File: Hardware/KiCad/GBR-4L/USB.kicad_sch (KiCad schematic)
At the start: 0 parts

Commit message: Add USB hub schematic
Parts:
- added C1: 4.7nF 1kV, Capacitor_SMD:C_1206_3216Metric, symbol Device:C
- added C10, C2, C3, C7, C8, C9: 100nF, Capacitor_SMD:C_0603_1608Metric, symbol Device:C
- added C11: 4.7uF, Capacitor_SMD:C_0805_2012Metric, symbol Device:C
- added C4, C5: 12pF C0G, Capacitor_SMD:C_0603_1608Metric, symbol Device:C
- added C6: 1uF, Capacitor_SMD:C_0603_1608Metric, symbol Device:C
- added J1: USB4105-GF-A, Connector_USB:USB_C_Receptacle_GCT_USB4105-xx-A_16P_TopMnt_Horizontal, symbol Connector:USB_C_Receptacle_USB2.0_16P
- added R1, R2: 5.1k 1%, Resistor_SMD:R_0603_1608Metric, symbol Device:R
- added R3: 1M, Resistor_SMD:R_0603_1608Metric, symbol Device:R
- added R4, R5: 100k 1%, Resistor_SMD:R_0603_1608Metric, symbol Device:R
- added R6: 12.0k 1%, Resistor_SMD:R_0603_1608Metric, symbol Device:R
- added R7: 10k, Resistor_SMD:R_0603_1608Metric, symbol Device:R
- added U1: USBLC6-2SC6, Package_TO_SOT_SMD:SOT-23-6, symbol Power_Protection:USBLC6-2SC6
- added U2: USB2514Bi-I/M2, Package_DFN_QFN:QFN-36-1EP_6x6mm_P0.5mm_EP4.1x4.1mm_ThermalVias, symbol Interface_USB:USB2514B_Bi
- added Y1: 24MHz, symbol Device:Crystal
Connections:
- new net +3V3_SYS: C10.1, C11.1, C7.1, C8.1, C9.1, R7.1, U2.10 (VDDA33), U2.15 (VDD33), U2.23 (VDD33), U2.29 (VDDA33), U2.36 (VDDA33), U2.5 (VDDA33)
- new net GND: C1.2, C10.2, C11.2, C2.2, C3.2, C4.2, C5.2, C6.2, C7.2, C8.2, C9.2, J1.A1 (GND), J1.A12 (GND), J1.B1 (GND), J1.B12 (GND), R1.2, R2.2, R3.2, R5.2, R6.2, U1.2 (GND), U2.37 (VSS)
- new net HUB_CRFILT: C2.1, U2.14 (CRFILT)
- new net HUB_PLLFILT: C3.1, U2.34 (PLLFILT)
- new net HUB_RBIAS: R6.1, U2.35 (RBIAS)
- new net HUB_RESET#: C6.1, R7.2, U2.26 (RESET_N)
- new net HUB_XTALIN: C4.1, U2.33 (XTALIN/CLKIN), Y1.1
- new net HUB_XTALOUT: C5.1, U2.32 (XTALOUT), Y1.2
- new net USB_CC1: J1.A5 (CC1), R1.1
- new net USB_CC2: J1.B5 (CC2), R2.1
- new net USB_M1_D+: U2.2 (USBDP_DN1/PRT_DIS_P1)
- new net USB_M1_D-: U2.1 (USBDM_DN1/PRT_DIS_M1)
- new net USB_M2_D+: U2.4 (USBDP_DN2/PRT_DIS_P2)
- new net USB_M2_D-: U2.3 (USBDM_DN2/PRT_DIS_M2)
- new net USB_M3_D+: U2.7 (USBDP_DN3/PRT_DIS_P3)
- new net USB_M3_D-: U2.6 (USBDM_DN3/PRT_DIS_M3)
- new net USB_M4_D+: U2.9 (USBDP_DN4/PRT_DIS_P4)
- new net USB_M4_D-: U2.8 (USBDM_DN4/PRT_DIS_M4)
- new net USB_SHIELD: C1.1, J1.SH (SHIELD), R3.1
- new net USB_UP_DM: U1.4 (I/O2), U2.30 (USBDM_UP)
- new net USB_UP_DM_CONN: J1.A7 (D-), J1.B7 (D-), U1.3 (I/O2)
- new net USB_UP_DP: U1.6 (I/O1), U2.31 (USBDP_UP)
- new net USB_UP_DP_CONN: J1.A6 (D+), J1.B6 (D+), U1.1 (I/O1)
- new net USB_VBUS: J1.A4 (VBUS), J1.A9 (VBUS), J1.B4 (VBUS), J1.B9 (VBUS), R4.1, U1.5 (VBUS)
- new net USB_VBUS_DET: R4.2, R5.1, U2.27 (VBUS_DET)
- no-connect marks 0 -> 15
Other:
- note added: "Default hub configuration is self-powered. All four downstream ports remain enabled."
- note added: "USB TYPE-C UPSTREAM (UFP, USB 2.0 ONLY)"
- note added: "USB2514B SELF-POWERED FOUR-PORT HUB"
- note added: "Use 90-ohm differential routing over continuous ground; avoid test-point stubs."
- note added: "VBUS is sense-only. Modems and hub are powered from the external 12 V supply."
- title: (none) -> GBR-4L USB hub

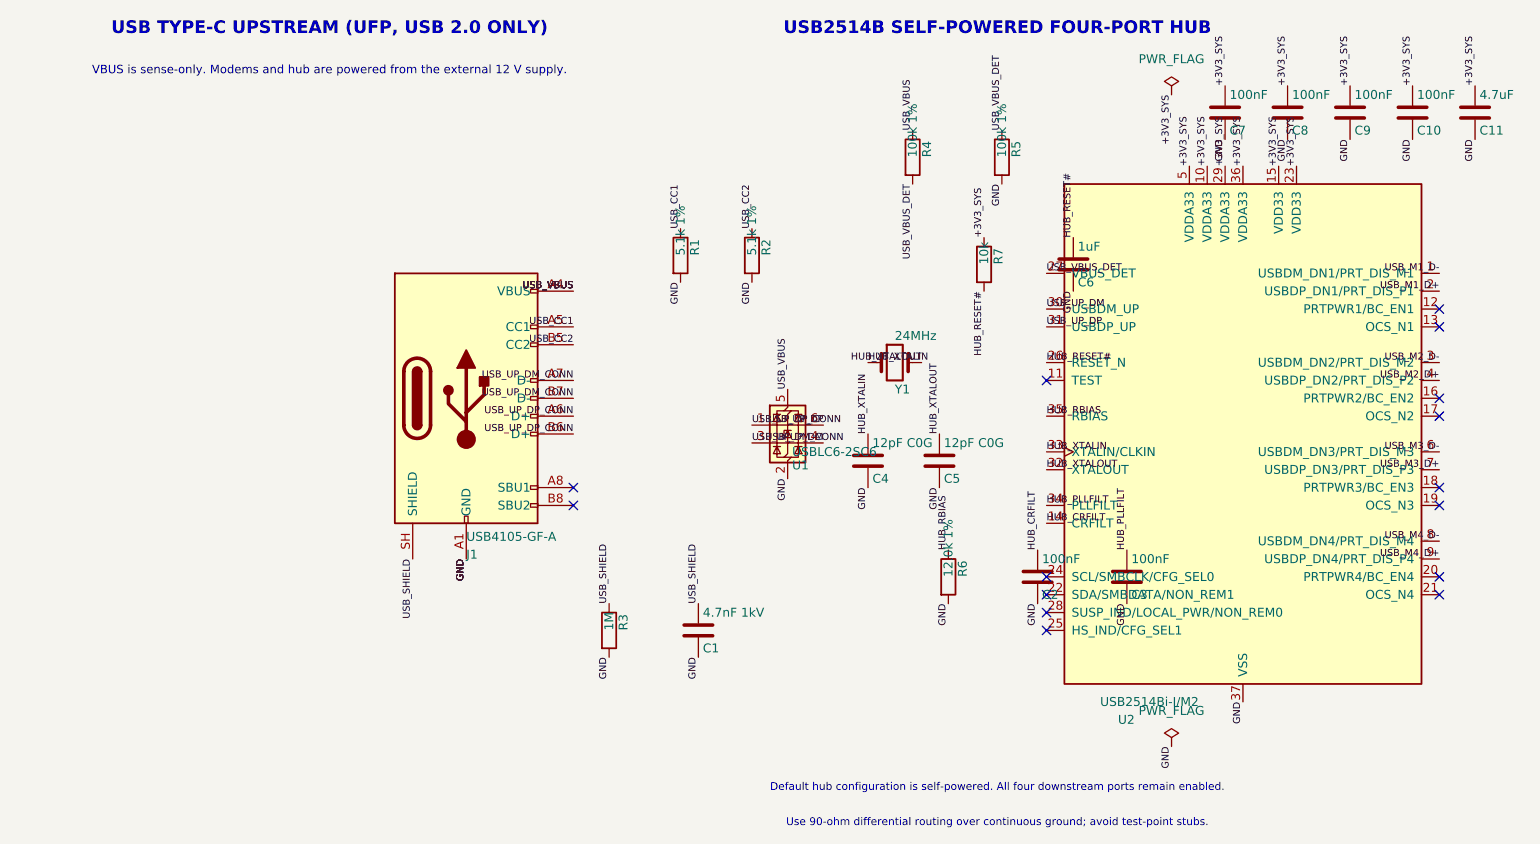
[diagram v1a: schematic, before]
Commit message: Add modem and SIM schematics
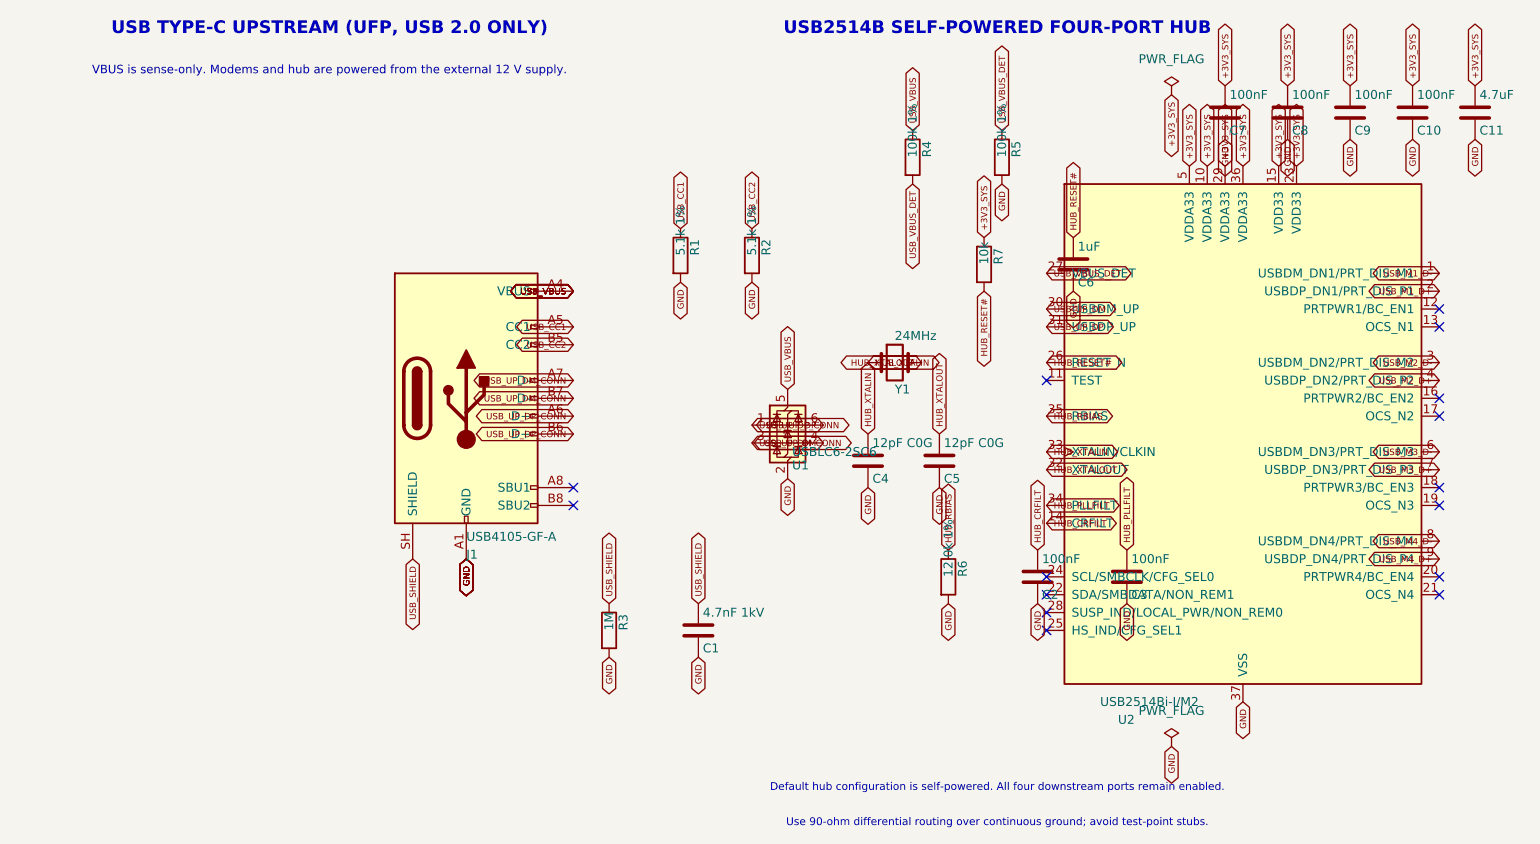
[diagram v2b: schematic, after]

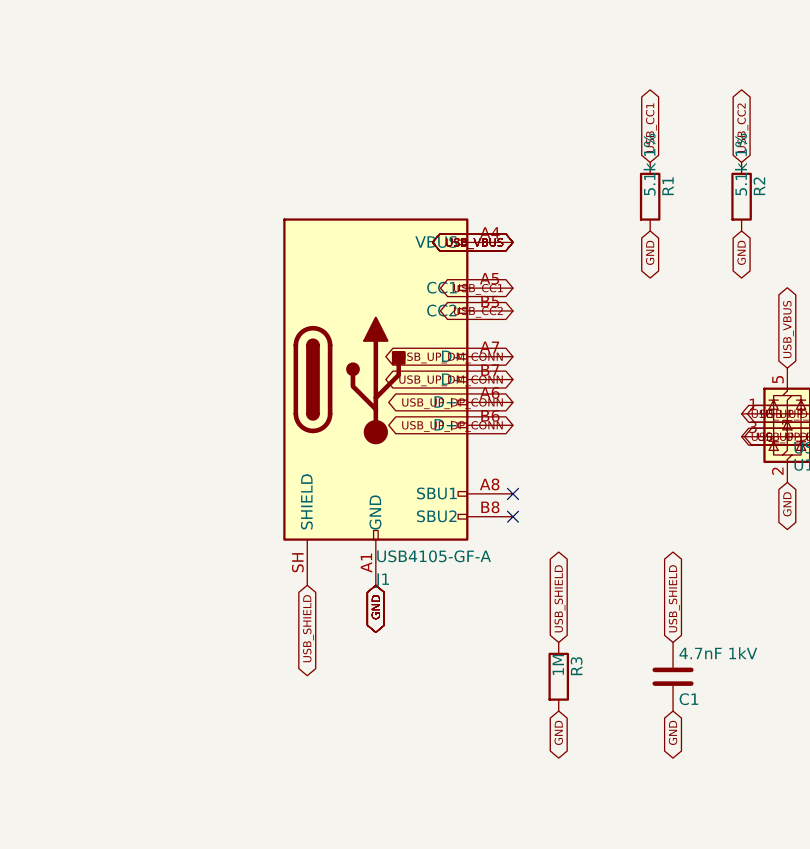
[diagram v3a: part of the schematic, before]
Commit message: Add connector footprints and initial PCB packing
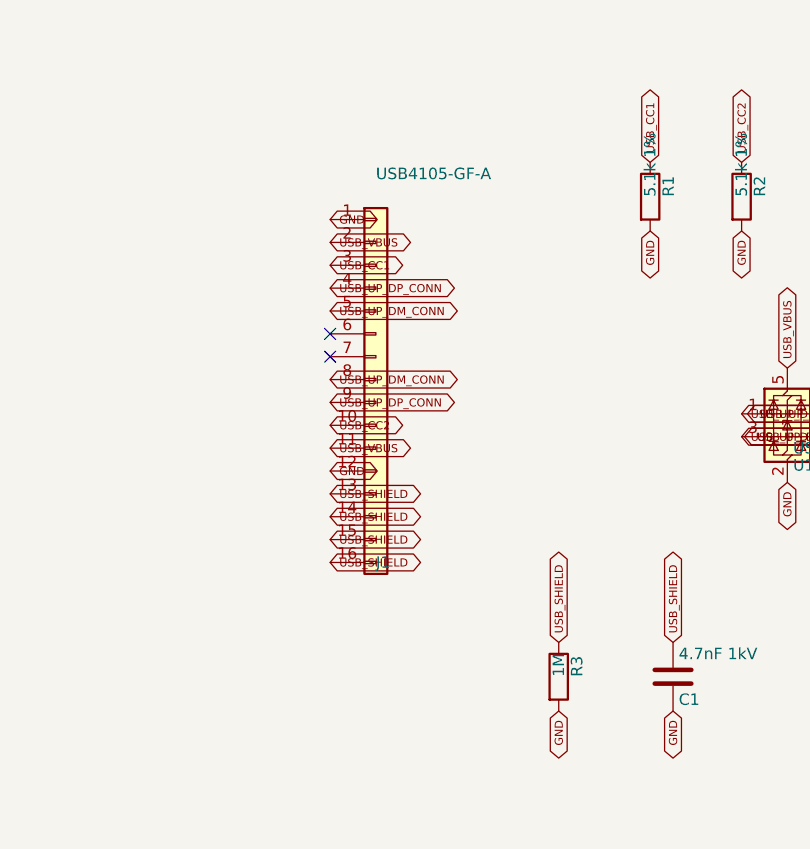
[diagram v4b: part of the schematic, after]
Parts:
- removed J1: USB4105-GF-A, Connector_USB:USB_C_Receptacle_GCT_USB4105-xx-A_16P_TopMnt_Horizontal, symbol Connector:USB_C_Receptacle_USB2.0_16P
- added J1: USB4105-GF-A, GBR-4L:GCT_USB4105-16P_MergedTails, symbol Connector_Generic:Conn_01x16
- U2: footprint Package_DFN_QFN:QFN-36-1EP_6x6mm_P0.5mm_EP4.1x4.1mm_ThermalVias -> Package_DFN_QFN:QFN-36-1EP_6x6mm_P0.5mm_EP4.1x4.1mm
- Y1: footprint (none) -> Crystal:Crystal_SMD_3225-4Pin_3.2x2.5mm
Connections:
- net GND: now also J1.1 (Pin_1), J1.12 (Pin_12)
- net USB_CC1: now also J1.3 (Pin_3)
- net USB_CC2: now also J1.10 (Pin_10)
- net USB_SHIELD: now also J1.13 (Pin_13), J1.14 (Pin_14), J1.15 (Pin_15), J1.16 (Pin_16)
- net USB_UP_DM_CONN: now also J1.5 (Pin_5), J1.8 (Pin_8)
- net USB_UP_DP_CONN: now also J1.4 (Pin_4), J1.9 (Pin_9)
- net USB_VBUS: now also J1.11 (Pin_11), J1.2 (Pin_2)
